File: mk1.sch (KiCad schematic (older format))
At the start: 19 parts, among them J1 USB, P1 BUS1, P2 BUS2, P3 BUS3, SW1 RESET, U1 WD65C02, U2 AT28C64B, U3 CY7C199, U4 74HC132

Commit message: tidy up schematic
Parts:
- removed U2: AT28C64B, symbol CY7C199
- added C5: 10nF, ~, symbol C
- added P4: ICP, symbol CONN_5
- added U2: AT28C64B, ~, symbol AT28C64B
- added unit 2 of U4
- added unit 3 of U4
- added unit 4 of U4
- renumbered P3 to P1, P1 to P2, P2 to P3
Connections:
- net labels added: ICP OE, VCC, ~ROM OE, ~ROM WE
- net labels removed: A[0..15], CONTROL, D[0..7]
- wire segments 166 -> 204
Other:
- note added: "AT U4\n"
- note added: "A[0..15]"
- note added: "CONTROL"
- note added: "D[0..7]"
- note added: "RAM $0000-$8000 (BOTTOM 32K)\nROM $C000-$FFFF (TOP 8K)"
- note added: "SHORT P4\n1&2, 3&4 STD\n2&3, 4&5 ICP"
- moved on the sheet: C1, C2, C3, C4, D1, J1, P1, P2, P3, R1, R2, R3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

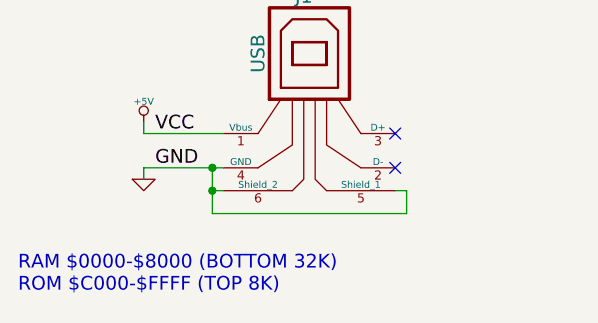
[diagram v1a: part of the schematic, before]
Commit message: fix memory map for ROM
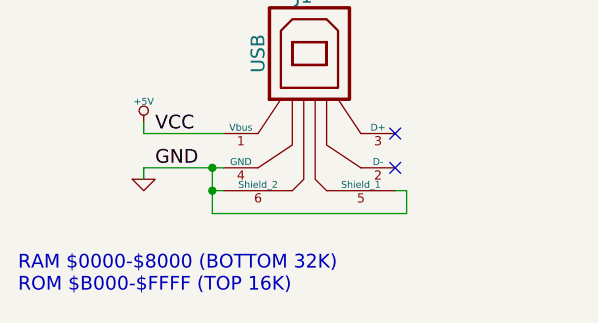
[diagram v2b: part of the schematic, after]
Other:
- note added: "RAM $0000-$8000 (BOTTOM 32K)\nROM $B000-$FFFF (TOP 16K)"
- note removed: "RAM $0000-$8000 (BOTTOM 32K)\nROM $C000-$FFFF (TOP 8K)"
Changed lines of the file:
@@
 $EndComp
 Text Notes 550  7650 0    60   ~ 0
-RAM $0000-$8000 (BOTTOM 32K)\nROM $C000-$FFFF (TOP 8K)
+RAM $0000-$8000 (BOTTOM 32K)\nROM $B000-$FFFF (TOP 16K)
 Text Label 3300 3950 1    60   ~ 0
 PHI2

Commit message: fix address and ICP logic
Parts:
- removed P4: ICP, symbol CONN_5
- removed U2: AT28C64B, ~, symbol AT28C64B
- added P5: ICP SEL, symbol CONN_3X2
- added U2: AT28C256, ~, symbol AT28C256
- added U5: MXO45HS, symbol MXO45HS
- P1: value BUS3 -> BUS 1
- P2: value BUS1 -> BUS 2
- P3: value BUS2 -> BUS 3
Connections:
- net labels added: CLK
- net labels removed: ICP OE, PHI0
- wire segments 204 -> 211
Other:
- note added: "FOR ICP, SHORT 3&5, 4&6\nPULL ~RST~ LOW\nUSE ~IRQ~=~WE~, A14=~OE~"
- note added: "FOR STANDARD BEHAVIOUR,\nSHORT 1&3, 2&4\n"
- note added: "MEMORY MAP\n$0000-$7FFF RAM (32K)\n$8000-$AFFF I/O (16K)\n$B000-$FFFF ROM (16K)"
- note removed: "RAM $0000-$8000 (BOTTOM 32K)\nROM $B000-$FFFF (TOP 16K)"
- note removed: "SHORT P4\n1&2, 3&4 STD\n2&3, 4&5 ICP"
- moved on the sheet: C1, C2, C3, C4, C5, D1, J1, P1, P3, R1, R2, R3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

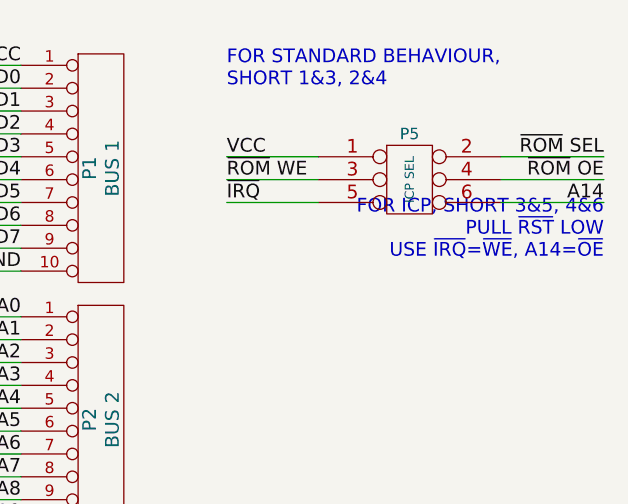
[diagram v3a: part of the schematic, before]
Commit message: move to using R/~W for ~WE
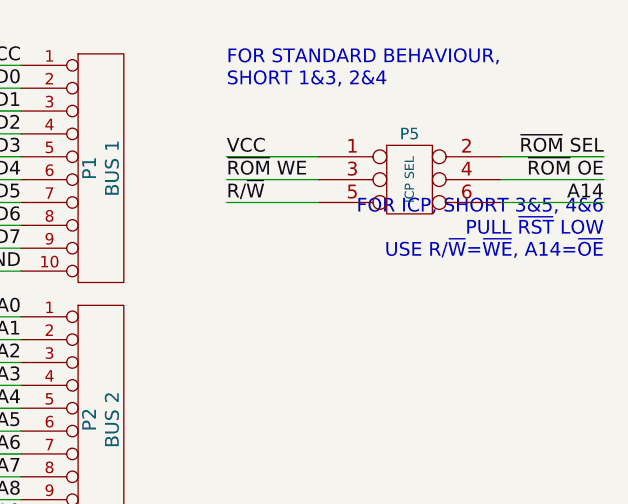
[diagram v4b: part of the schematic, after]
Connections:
- net R/~W: now also P5.5
- net ~IRQ: no longer P5.5
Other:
- note added: "FOR ICP, SHORT 3&5, 4&6\nPULL ~RST~ LOW\nUSE R/~W~=~WE~, A14=~OE~"
- note removed: "FOR ICP, SHORT 3&5, 4&6\nPULL ~RST~ LOW\nUSE ~IRQ~=~WE~, A14=~OE~"
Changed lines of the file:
@@
 	9700 1650 9300 1650
 Text Label 9300 1750 0    60   ~ 0
-~IRQ
+R/~W
 Text Label 10950 1750 2    60   ~ 0
 A14
@@
 	6650 6700 6550 6700
 Text Notes 10950 2000 2    60   ~ 0
-FOR ICP, SHORT 3&5, 4&6\nPULL ~RST~ LOW\nUSE ~IRQ~=~WE~, A14=~OE~
+FOR ICP, SHORT 3&5, 4&6\nPULL ~RST~ LOW\nUSE R/~W~=~WE~, A14=~OE~
 Entry Wire Line
 	3900 4550 4000 4650

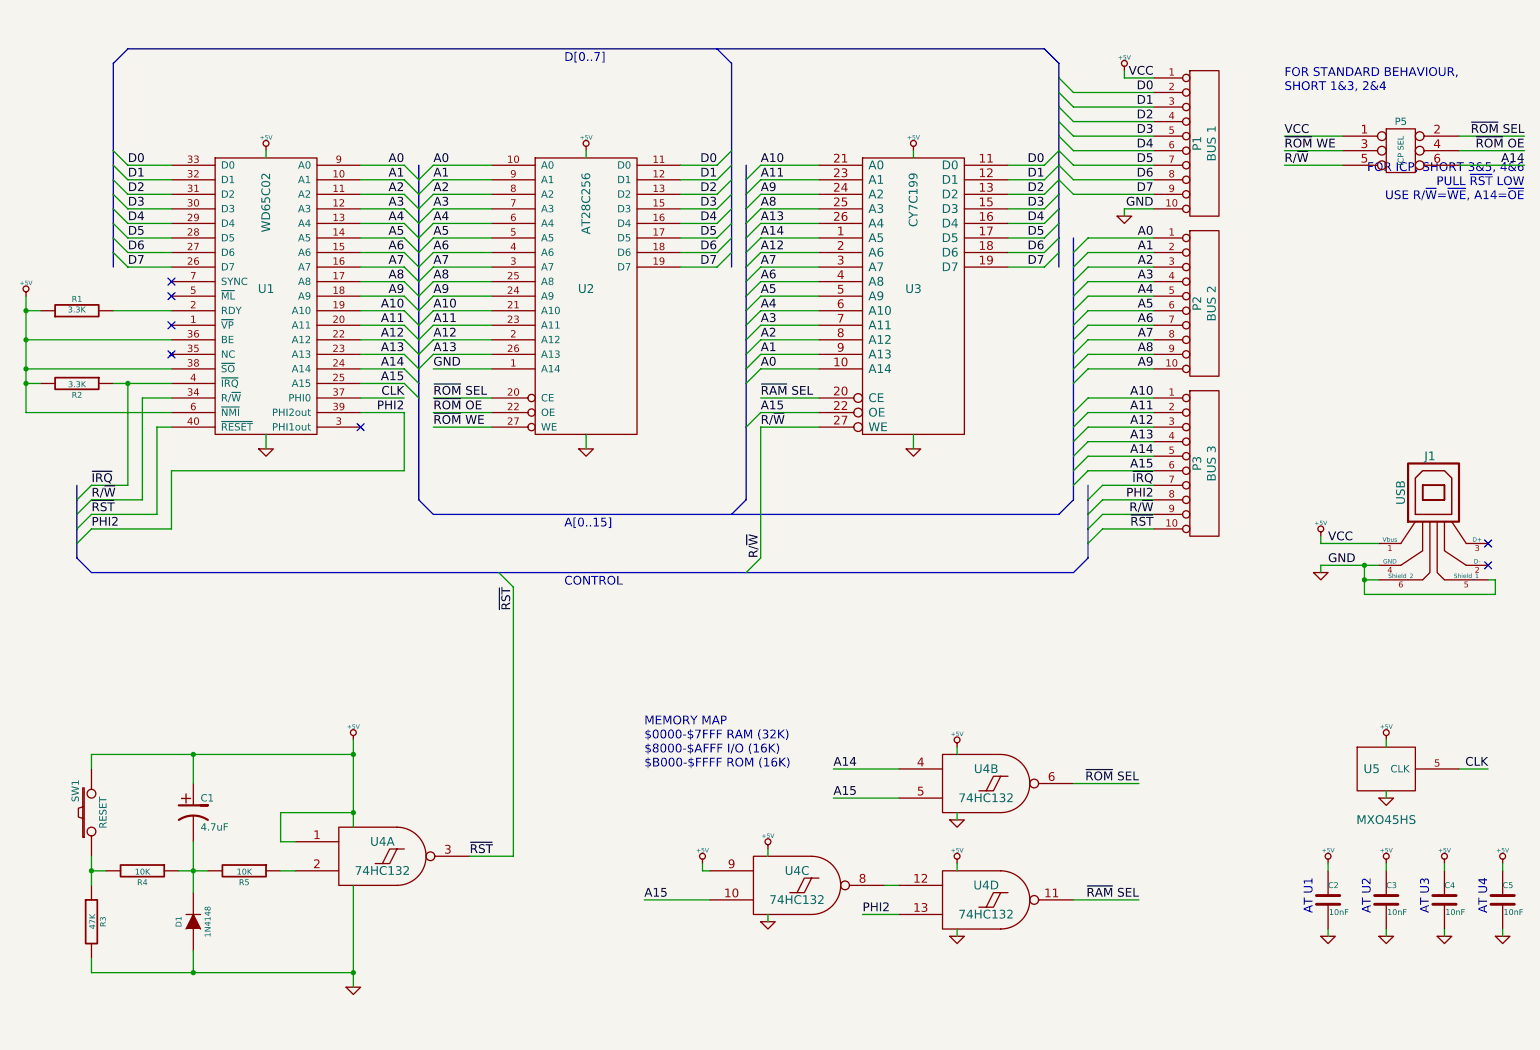
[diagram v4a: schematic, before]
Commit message: tidy up layout a lot
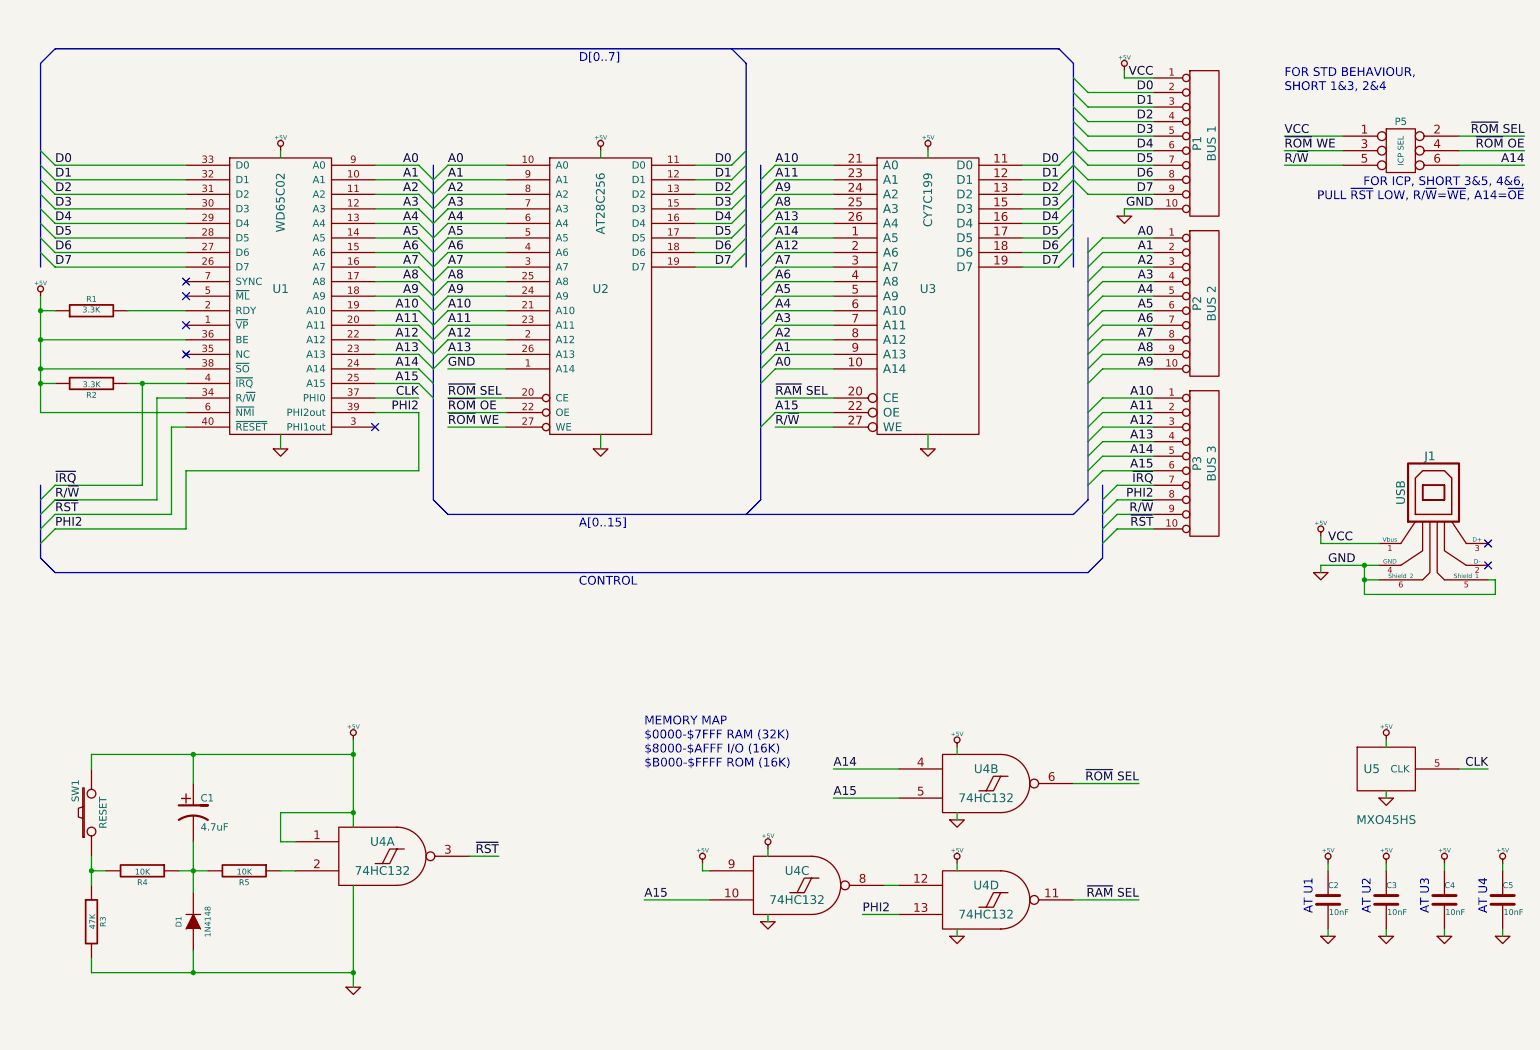
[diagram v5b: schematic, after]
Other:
- note added: "FOR ICP, SHORT 3&5, 4&6,\nPULL ~RST~ LOW, R/~W~=~WE~, A14=~OE~"
- note added: "FOR STD BEHAVIOUR,\nSHORT 1&3, 2&4"
- note removed: "FOR ICP, SHORT 3&5, 4&6\nPULL ~RST~ LOW\nUSE R/~W~=~WE~, A14=~OE~"
- note removed: "FOR STANDARD BEHAVIOUR,\nSHORT 1&3, 2&4\n"
- moved on the sheet: R1, R2, U1, U2, U3
